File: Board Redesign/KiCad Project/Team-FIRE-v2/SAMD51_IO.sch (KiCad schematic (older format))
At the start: 20 parts, among them U5 SAMD51, Y1 32.768kHz

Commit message: Labelled finished sections on schematic, picked LEDs
- Labelled all finished schematic sections if they've been part-selected / verified (and by whom)
- Selected the four debug LEDs and filled out BOM info
- Filled out info for Power/TES connectors
- Filled out info for RF connector
- Filled out info for 5 to 3.3V regulator
- Filled out info for 8 to 5V switching regulator
- Assigned footprints to test points
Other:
- note added: "PART SELECTION FINISHED - COLLIN"
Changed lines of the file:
@@
 Wire Notes Line
 	3750 6700 3750 5850
+Text Notes 3700 6850 0    79   ~ 16
+PART SELECTION FINISHED - COLLIN
+Text Notes 3750 5500 0    79   ~ 16
+PART SELECTION FINISHED - COLLIN
 $EndSCHEMATC

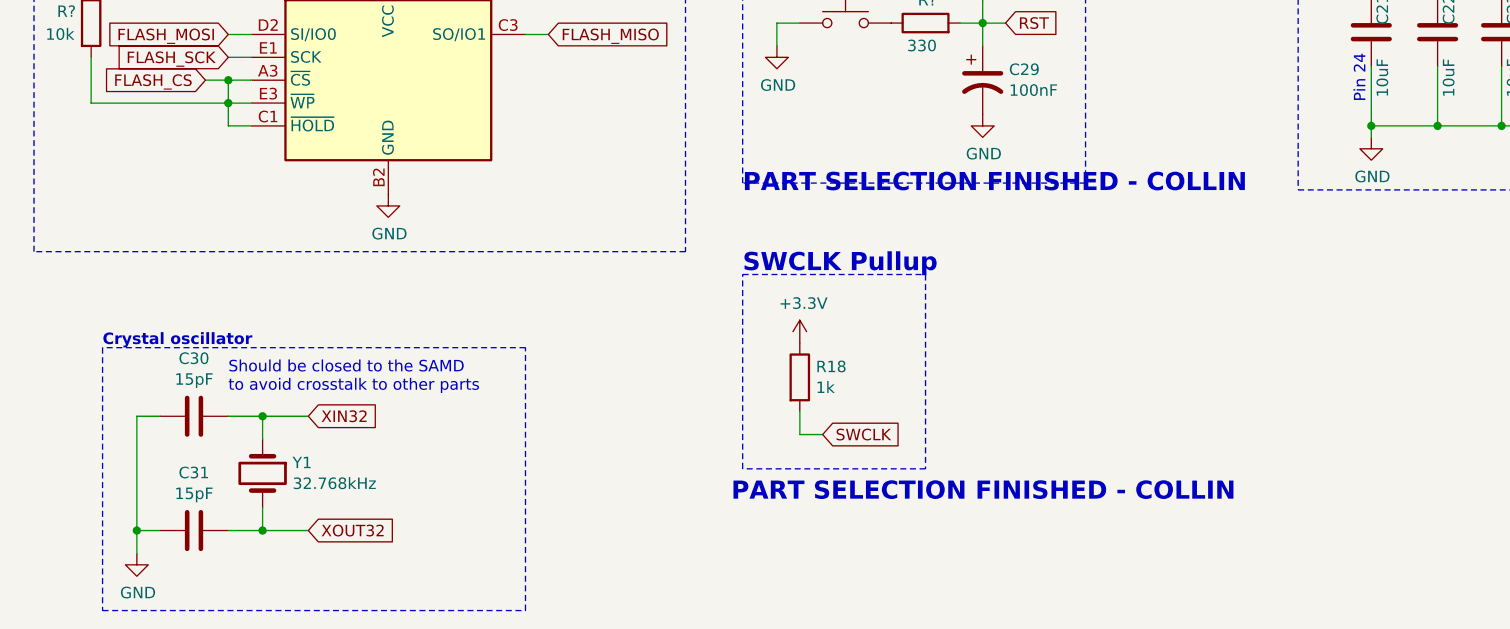
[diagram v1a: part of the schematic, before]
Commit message: Selected components for SAMD51
- Selected components for crystal oscillators
- Selected component for reset button
- Selected component for flash memory (cant find details for flash module...)
- Ran schematic annotation
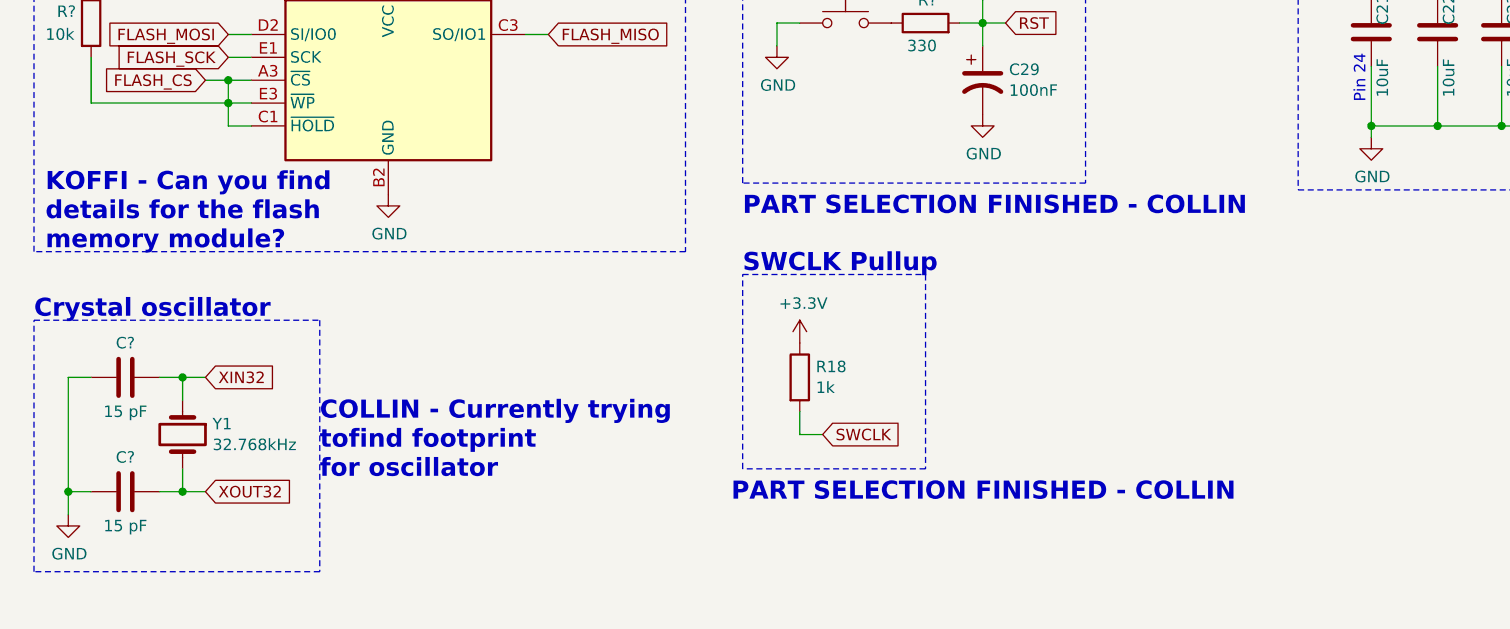
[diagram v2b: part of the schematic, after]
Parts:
- removed C30, C31: 15pF, symbol Device:C
- added C? (x2): 15 pF, Capacitor_SMD:C_0603_1608Metric, symbol Device:C
- C29: Link (none) -> https://www.mouser.com/ProductDetail/KEMET/C0603X104K5RAC33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; MPN (none) -> C0603X104K5RAC3316; Manufacturer (none) -> KEMET; Supplier (none) -> Mouser; Supplier PN (none) -> 80-C0603X104K5R3316; Tolerance (none) -> 10%; Type (none) -> Ceramic X7R Capacitor; Voltage Rating (none) -> 50 VDC
- SW?: Current Rating (none) -> 20 mA; Description (none) -> Reset button; Link (none) -> https://www.mouser.com/ProductDetail/Panasonic/EVQ-Q2Y03W?q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; Manufacturer (none) -> Panasonic; Supplier (none) -> Mouser; Supplier PN (none) -> 667-EVQ-Q2Y03W; Voltage Rating (none) -> 15 VDC, 250 VAC
- Y1: Description (none) -> 32.768 kHz Oscillator; Link (none) -> https://www.mouser.com/ProductDetail/Renesas-IDT/XUH5350000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; MPN (none) -> XUH535000.032768I; Manufacturer (none) -> Renesas Electronics; Supplier (none) -> Mouser; Supplier PN (none) -> 972-XUH535000032768I; Voltage Rating (none) -> 3.135 to 3.465 V
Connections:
- net GND: now also C?.2, C?.2
- net XIN32: now also C?.1
- net XOUT32: now also C?.1
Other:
- note added: "COLLIN - Currently trying\ntofind footprint\nfor oscillator"
- note added: "KOFFI - Can you find\ndetails for the flash\nmemory module?"
- note removed: "Should be closed to the SAMD \nto avoid crosstalk to other parts"
- moved on the sheet: Y1
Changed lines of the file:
@@
 L Device:Crystal Y?
 U 1 1 5F15C3C7
-P 1650 6720
+P 1300 6550
 AR Path="/5E4F8378/5F15C3C7" Ref="Y?"  Part="1"
 AR Path="/5E4F8378/5EA71818/5F15C3C7" Ref="Y?"  Part="1"
 AR Path="/5E4F8378/5ED4DEFC/5ED7D75E/5F15C3C7" Ref="Y?"  Part="1"
 AR Path="/5E4F8378/5ED4DEFC/5F15C3C7" Ref="Y1"  Part="1"
-F 0 "Y1" V 1604 6851 50  0000 L CNN
-F 1 "32.768kHz" V 1695 6851 50  0000 L CNN
-F 2 "" H 1650 6720 50  0001 C CNN
-F 3 "~" H 1650 6720 50  0001 C CNN
-	1    1650 6720
+F 0 "Y1" V 1254 6681 50  0000 L CNN
+F 1 "32.768kHz" V 1345 6681 50  0000 L CNN
+F 2 "" H 1300 6550 50  0001 C CNN
+F 3 "https://www.mouser.com/ProductDetail/Renesas-IDT/XUH535000032768I?qs=sGAEpiMZZMt8zWNA7msRCkfKROQbNyT9ksyE2KEVrnhTAWaYHdZ16w%3D%3D" H 1300 6550 50  0001 C CNN
+F 4 "XUH535000.032768I" V 1300 6550 50  0001 C CNN "MPN"
+F 5 "Renesas Electronics" V 1300 6550 50  0001 C CNN "Manufacturer"
+F 6 "Mouser" V 1300 6550 50  0001 C CNN "Supplier"
+F 7 "972-XUH535000032768I" V 1300 6550 50  0001 C CNN "Supplier PN"
+F 8 "https://www.mouser.com/ProductDetail/Renesas-IDT/XUH535000032768I?qs=sGAEpiMZZMt8zWNA7msRCkfKROQbNyT9ksyE2KEVrnhTAWaYHdZ16w%3D%3D" V 1300 6550 50  0001 C CNN "Link"
+F 9 "3.135 to 3.465 V" V 1300 6550 50  0001 C CNN "Voltage Rating"
+F 10 "32.768 kHz Oscillator" V 1300 6550 50  0001 C CNN "Description"
+	1    1300 6550
 	0    1    1    0
-$EndComp
-$Comp
-L Device:C C?
-U 1 1 5F15C3CD
-P 1350 6470
-AR Path="/5E4F8378/5F15C3CD" Ref="C?"  Part="1"
-AR Path="/5E4F8378/5EA71818/5F15C3CD" Ref="C?"  Part="1"
-AR Path="/5E4F8378/5ED4DEFC/5ED7D75E/5F15C3CD" Ref="C?"  Part="1"
-AR Path="/5E4F8378/5ED4DEFC/5F15C3CD" Ref="C30"  Part="1"
-F 0 "C30" V 1098 6470 50  0000 C CNN
-F 1 "15pF" V 1189 6470 50  0000 C CNN
-F 2 "" H 1388 6320 50  0001 C CNN
-F 3 "~" H 1350 6470 50  0001 C CNN
-	1    1350 6470
-	0    1    1    0
-$EndComp
-$Comp
-L Device:C C?
-U 1 1 5F15C3D3
-P 1350 6970
-AR Path="/5E4F8378/5F15C3D3" Ref="C?"  Part="1"
-AR Path="/5E4F8378/5EA71818/5F15C3D3" Ref="C?"  Part="1"
-AR Path="/5E4F8378/5ED4DEFC/5ED7D75E/5F15C3D3" Ref="C?"  Part="1"
-AR Path="/5E4F8378/5ED4DEFC/5F15C3D3" Ref="C31"  Part="1"
-F 0 "C31" V 1602 6970 50  0000 C CNN
-F 1 "15pF" V 1511 6970 50  0000 C CNN
-F 2 "" H 1388 6820 50  0001 C CNN
-F 3 "~" H 1350 6970 50  0001 C CNN
-	1    1350 6970
-	0    -1   -1   0
 $EndComp
 $Comp
 L power:GND #PWR?
 U 1 1 5F15C3D9
-P 1100 7070
+P 800 6900
 AR Path="/5E4F8378/5F15C3D9" Ref="#PWR?"  Part="1"
 AR Path="/5E4F8378/5EA71818/5F15C3D9" Ref="#PWR?"  Part="1"
 AR Path="/5E4F8378/5ED4DEFC/5ED7D75E/5F15C3D9" Ref="#PWR?"  Part="1"
 AR Path="/5E4F8378/5ED4DEFC/5F15C3D9" Ref="#PWR0152"  Part="1"
-F 0 "#PWR0152" H 1100 6820 50  0001 C CNN
-F 1 "GND" H 1105 6897 50  0000 C CNN
-F 2 "" H 1100 7070 50  0001 C CNN
-F 3 "" H 1100 7070 50  0001 C CNN
-	1    1100 7070
-	1    0    0    -1
-$EndComp
-Text GLabel 1850 6970 2    50   Input ~ 0
+F 0 "#PWR0152" H 800 6650 50  0001 C CNN
+F 1 "GND" H 805 6727 50  0000 C CNN
+F 2 "" H 800 6900 50  0001 C CNN
+F 3 "" H 800 6900 50  0001 C CNN
+	1    800  6900
+	1    0    0    -1
+$EndComp
+Text GLabel 1400 6800 2    50   Input ~ 0
 XOUT32
-Wire Notes Line
-	950  7320 2800 7320
-Wire Notes Line
-	2800 7320 2800 6170
-Wire Notes Line
-	2800 6170 950  6170
-Wire Notes Line
-	950  6170 950  7320
-Text Notes 950  6170 0    50   ~ 10
-Crystal oscillator
-Text Notes 1500 6370 0    50   ~ 0
-Should be closed to the SAMD \nto avoid crosstalk to other parts
-Wire Wire Line
-	1500 6470 1650 6470
-Wire Wire Line
-	1650 6570 1650 6470
-Connection ~ 1650 6470
-Wire Wire Line
-	1650 6470 1850 6470
-Wire Wire Line
-	1500 6970 1650 6970
-Wire Wire Line
-	1650 6870 1650 6970
-Connection ~ 1650 6970
-Wire Wire Line
-	1650 6970 1850 6970
-Wire Wire Line
-	1200 6470 1100 6470
-Wire Wire Line
-	1100 6470 1100 6970
-Wire Wire Line
-	1100 6970 1200 6970
-Wire Wire Line
-	1100 6970 1100 7070
-Connection ~ 1100 6970
 $Comp
 L power:+3.3V #PWR?
@@
 F 1 "100nF" H 4915 4955 50  0000 L CNN
 F 2 "Capacitor_SMD:C_0603_1608Metric" H 4800 5000 50  0001 C CNN
-F 3 "~" H 4800 5000 50  0001 C CNN
+F 3 "https://www.mouser.com/datasheet/2/212/KEM_X7R_FT_VW_AUDI-1775098.pdf" H 4800 5000 50  0001 C CNN
+F 4 "C0603X104K5RAC3316" H 4800 5000 50  0001 C CNN "MPN"
+F 5 "KEMET" H 4800 5000 50  0001 C CNN "Manufacturer"
+F 6 "Mouser" H 4800 5000 50  0001 C CNN "Supplier"
+F 7 "80-C0603X104K5R3316" H 4800 5000 50  0001 C CNN "Supplier PN"
+F 8 "https://www.mouser.com/ProductDetail/KEMET/C0603X104K5RAC3316?qs=sGAEpiMZZMsh%252B1woXyUXj34sxNWs20QAoBWDPDKnR18%3D" H 4800 5000 50  0001 C CNN "Link"
+F 9 "Ceramic X7R Capacitor" H 4800 5000 50  0001 C CNN "Type"
+F 10 "10%" H 4800 5000 50  0001 C CNN "Tolerance"
+F 11 "50 VDC" H 4800 5000 50  0001 C CNN "Voltage Rating"
 	1    4800 5000
 	1    0    0    -1
@@
 NoConn ~ 1260 1390
 NoConn ~ 1260 1490
-Text GLabel 1850 6470 2    50   Input ~ 0
+Text GLabel 1400 6300 2    50   Input ~ 0
 XIN32
 $Comp
@@
 F 1 "RESET" H 4200 4944 50  0000 C CNN
 F 2 "Button_Switch_SMD:SW_SPST_EVQQ2" H 4200 4950 50  0001 C CNN
-F 3 "~" H 4200 4950 50  0001 C CNN
+F 3 "https://www.mouser.com/datasheet/2/315/sw_lt_eng_6s_th-1289042.pdf" H 4200 4950 50  0001 C CNN
 F 4 "EVQ-Q2Y03W" H 4200 4750 50  0001 C CNN "MPN"
+F 5 "Panasonic" H 4200 4750 50  0001 C CNN "Manufacturer"
+F 6 "Mouser" H 4200 4750 50  0001 C CNN "Supplier"
+F 7 "667-EVQ-Q2Y03W" H 4200 4750 50  0001 C CNN "Supplier PN"
+F 8 "https://www.mouser.com/ProductDetail/Panasonic/EVQ-Q2Y03W?qs=Ow%252BOiPmaljHytan%2FbFuZzg%3D%3D" H 4200 4750 50  0001 C CNN "Link"
+F 9 "15 VDC, 250 VAC" H 4200 4750 50  0001 C CNN "Voltage Rating"
+F 10 "20 mA" H 4200 4750 50  0001 C CNN "Current Rating"
+F 11 "Reset button" H 4200 4750 50  0001 C CNN "Description"
 	1    4200 4750
 	1    0    0    -1
@@
 Text Notes 3700 6850 0    79   ~ 16
 PART SELECTION FINISHED - COLLIN
-Text Notes 3750 5500 0    79   ~ 16
+Text Notes 3750 5600 0    79   ~ 16
 PART SELECTION FINISHED - COLLIN
+Text Notes 650  6050 0    79   ~ 16
+Crystal oscillator
+$Comp
+L Device:C C?
+U 1 1 5EB3DB6A
+P 1050 6300
+F 0 "C?" V 900 6300 50  0000 C CNN
+F 1 "15 pF" V 1200 6300 50  0000 C CNN
+F 2 "Capacitor_SMD:C_0603_1608Metric" H 1088 6150 50  0001 C CNN
+F 3 "https://www.mouser.com/datasheet/2/40/AVX_09302019_U_Dielectric_B_Termination_C0G_NP0-1658719.pdf" H 1050 6300 50  0001 C CNN
+F 4 "LD032U3R3BAB2A" H 1050 6300 50  0001 C CNN "MPN"
+F 5 "AVX" H 1050 6300 50  0001 C CNN "Manufacturer"
+F 6 "Mouser" H 1050 6300 50  0001 C CNN "Supplier"
+F 7 "581-LD032U3R3BAB2A" H 1050 6300 50  0001 C CNN "Supplier PN"
+F 8 "https://www.mouser.com/ProductDetail/AVX/LD032U3R3BAB2A?qs=r09KxNuG0AVh%2F1rBpEisGg%3D%3D" H 1050 6300 50  0001 C CNN "Link"
+F 9 "Ceramic C0G Capacitor" H 1050 6300 50  0001 C CNN "Type"
+F 10 "0.1 pF" H 1050 6300 50  0001 C CNN "Tolerance"
+F 11 "200 VDC" H 1050 6300 50  0001 C CNN "Voltage Rating"
+	1    1050 6300
+	0    1    1    0
+$EndComp
+$Comp
+L Device:C C?
+U 1 1 5EB44811
+P 1050 6800
+F 0 "C?" V 900 6800 50  0000 C CNN
+F 1 "15 pF" V 1200 6800 50  0000 C CNN
+F 2 "Capacitor_SMD:C_0603_1608Metric" H 1088 6650 50  0001 C CNN
+F 3 "https://www.mouser.com/datasheet/2/40/AVX_09302019_U_Dielectric_B_Termination_C0G_NP0-1658719.pdf" H 1050 6800 50  0001 C CNN
+F 4 "LD032U3R3BAB2A" H 1050 6800 50  0001 C CNN "MPN"
+F 5 "AVX" H 1050 6800 50  0001 C CNN "Manufacturer"
+F 6 "Mouser" H 1050 6800 50  0001 C CNN "Supplier"
+F 7 "581-LD032U3R3BAB2A" H 1050 6800 50  0001 C CNN "Supplier PN"
+F 8 "https://www.mouser.com/ProductDetail/AVX/LD032U3R3BAB2A?qs=r09KxNuG0AVh%2F1rBpEisGg%3D%3D" H 1050 6800 50  0001 C CNN "Link"
+F 9 "Ceramic C0G Capacitor" H 1050 6800 50  0001 C CNN "Type"
+F 10 "0.1 pF" H 1050 6800 50  0001 C CNN "Tolerance"
+F 11 "200 VDC" H 1050 6800 50  0001 C CNN "Voltage Rating"
+	1    1050 6800
+	0    1    1    0
+$EndComp
+Wire Wire Line
+	1200 6300 1300 6300
+Wire Wire Line
+	1300 6300 1300 6400
+Wire Wire Line
+	1300 6700 1300 6800
+Wire Wire Line
+	1300 6800 1200 6800
+Wire Wire Line
+	1400 6800 1300 6800
+Connection ~ 1300 6800
+Wire Wire Line
+	1300 6300 1400 6300
+Connection ~ 1300 6300
+Wire Wire Line
+	900  6300 800  6300
+Wire Wire Line
+	800  6300 800  6800
+Wire Wire Line
+	900  6800 800  6800
+Connection ~ 800  6800
+Wire Wire Line
+	800  6800 800  6900
+Wire Notes Line
+	650  6050 1900 6050
+Wire Notes Line
+	1900 6050 1900 7150
+Wire Notes Line
+	1900 7150 650  7150
+Wire Notes Line
+	650  7150 650  6050
+Text Notes 700  5750 0    79   ~ 16
+KOFFI - Can you find\ndetails for the flash\nmemory module?
+Text Notes 1900 6750 0    79   ~ 16
+COLLIN - Currently trying\ntofind footprint\nfor oscillator
 $EndSCHEMATC
